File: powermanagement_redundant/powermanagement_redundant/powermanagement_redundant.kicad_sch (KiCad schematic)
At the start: 48 parts, among them J1 Screw_Terminal_01x01, J2 Screw_Terminal_01x01, J3 Screw_Terminal_01x01, J4 Screw_Terminal_01x01, J5 Screw_Terminal_01x01, J6 Screw_Terminal_01x01, J7 Screw_Terminal_01x01, J8 Screw_Terminal_01x01, SW1 SW_DIP_x01, SW2 SW_DIP_x01

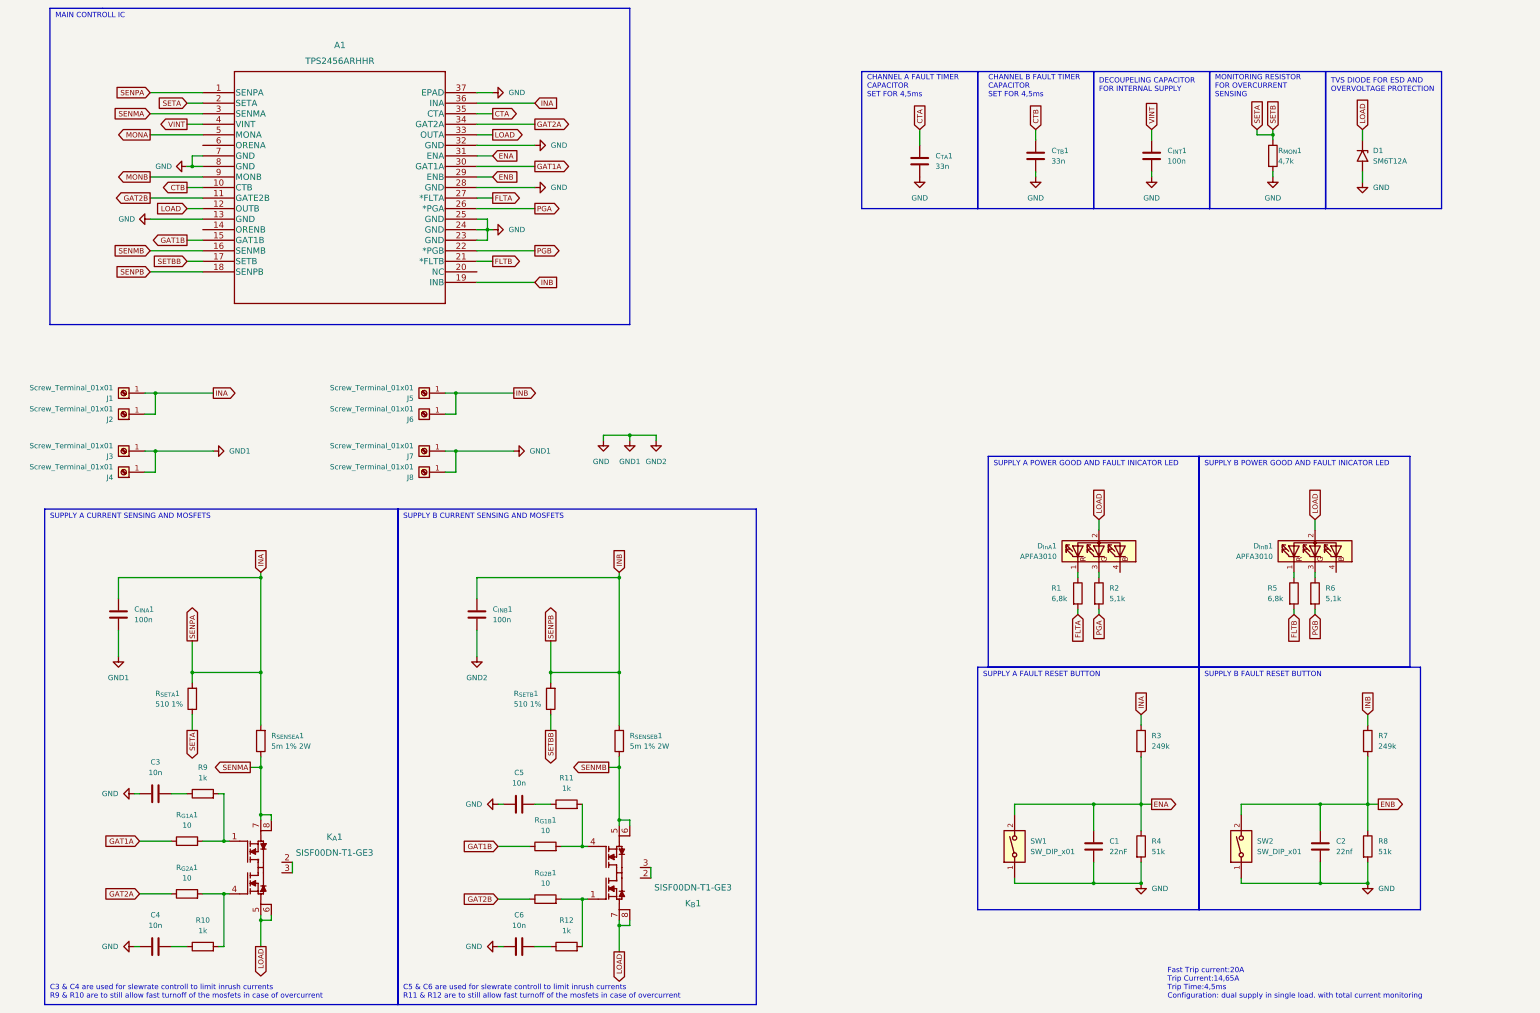
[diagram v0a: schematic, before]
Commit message: add PCB and make it for Aisler work
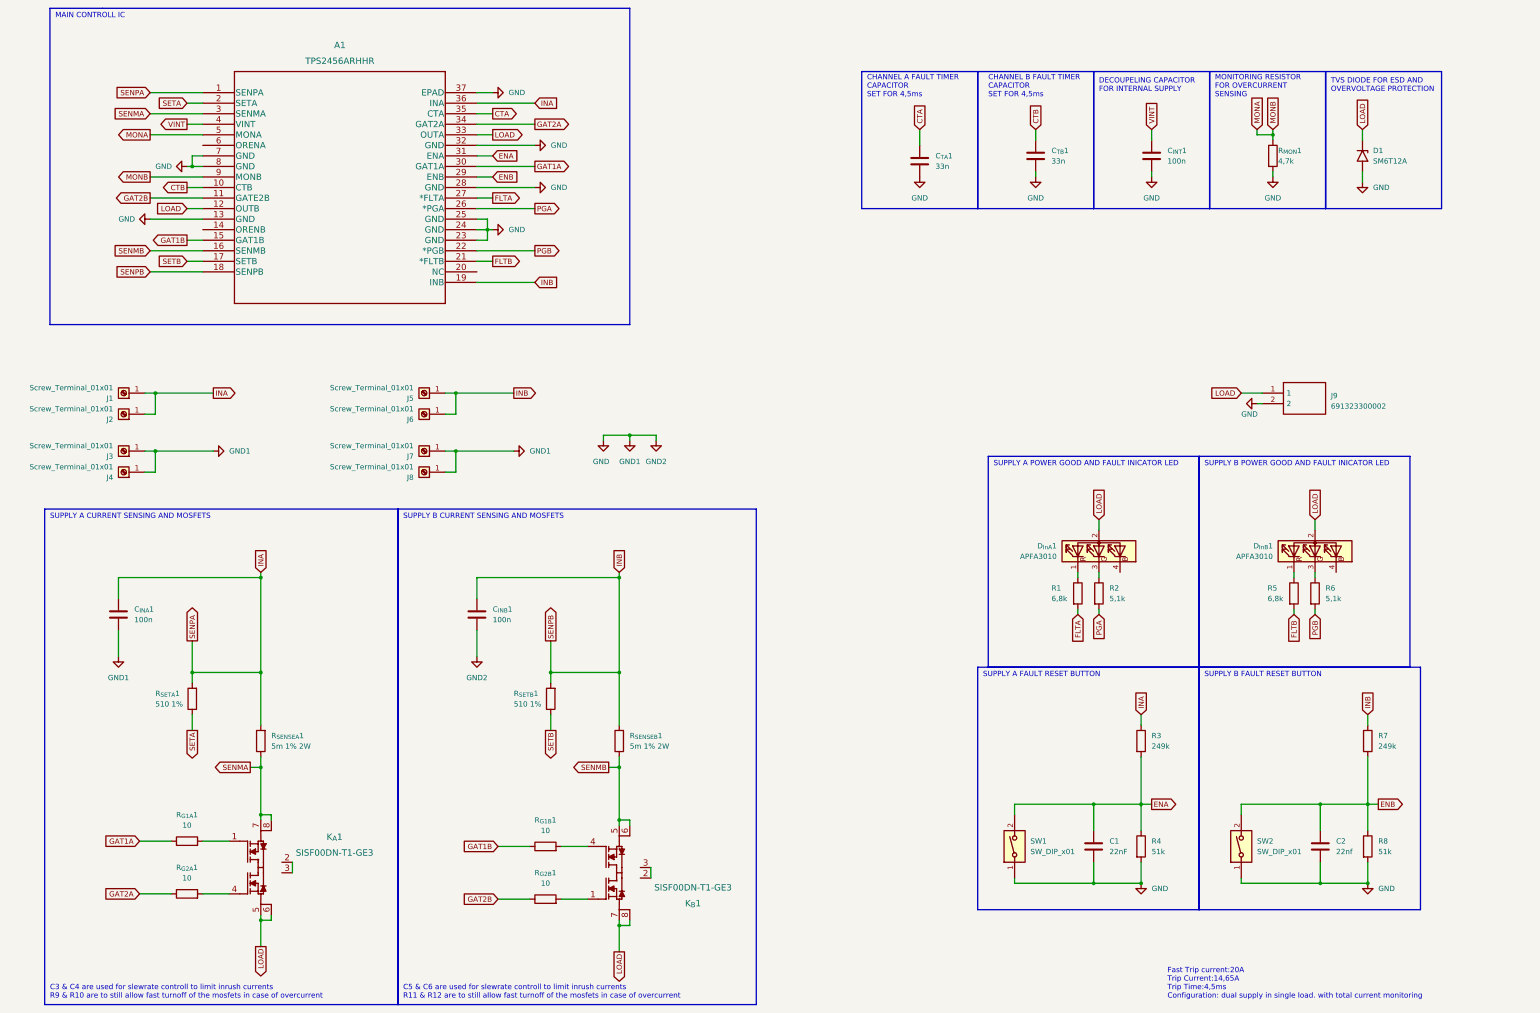
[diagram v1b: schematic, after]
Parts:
- removed C3, C4, C5, C6: 10n, Capacitor_SMD:C_0805_2012Metric_Pad1.18x1.45mm_HandSolder, symbol Device:C
- removed R10, R11, R12, R9: 1k, Resistor_SMD:R_0805_2012Metric_Pad1.20x1.40mm_HandSolder, symbol Device:R
- added J9: 691323300002, KiCad:691323300002, symbol 691323300002:691323300002
- C1, C2, C_{INA}1, C_{INB}1, C_{INT}1, C_{TA}1, C_{TB}1: footprint Capacitor_SMD:C_0805_2012Metric_Pad1.18x1.45mm_HandSolder -> Capacitor_SMD:C_0805_2012Metric
- R1, R2, R3, R4, R5, R6, R7, R8, R_{G1A}1, R_{G1B}1, R_{G2A}1, R_{G2B}1, R_{MON}1, R_{SETA}1, R_{SETB}1: footprint Resistor_SMD:R_0805_2012Metric_Pad1.20x1.40mm_HandSolder -> Resistor_SMD:R_0805_2012Metric
- R_{SENSEA}1, R_{SENSEB}1: footprint Resistor_SMD:R_0612_1632Metric_Pad1.18x3.40mm_HandSolder -> Resistor_SMD:R_0612_1632Metric
- SW1, SW2: footprint Button_Switch_SMD:Panasonic_EVQPUL_EVQPUC -> Button_Switch_SMD:Panasonic_EVQPUK_EVQPUB; Name EVQ-P7C01 -> EVQ-P7B01P
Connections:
- net MONB is gone; now on net MONA: A1.9 (MONB)
- net GND: now also J9.2
- net LOAD: now also J9.1
- net MONA: now also R_{MON}1.1
- net SETA: no longer R_{MON}1.1
- net SETBB renamed SETB

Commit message: upgrade mosfet footprint, change some values
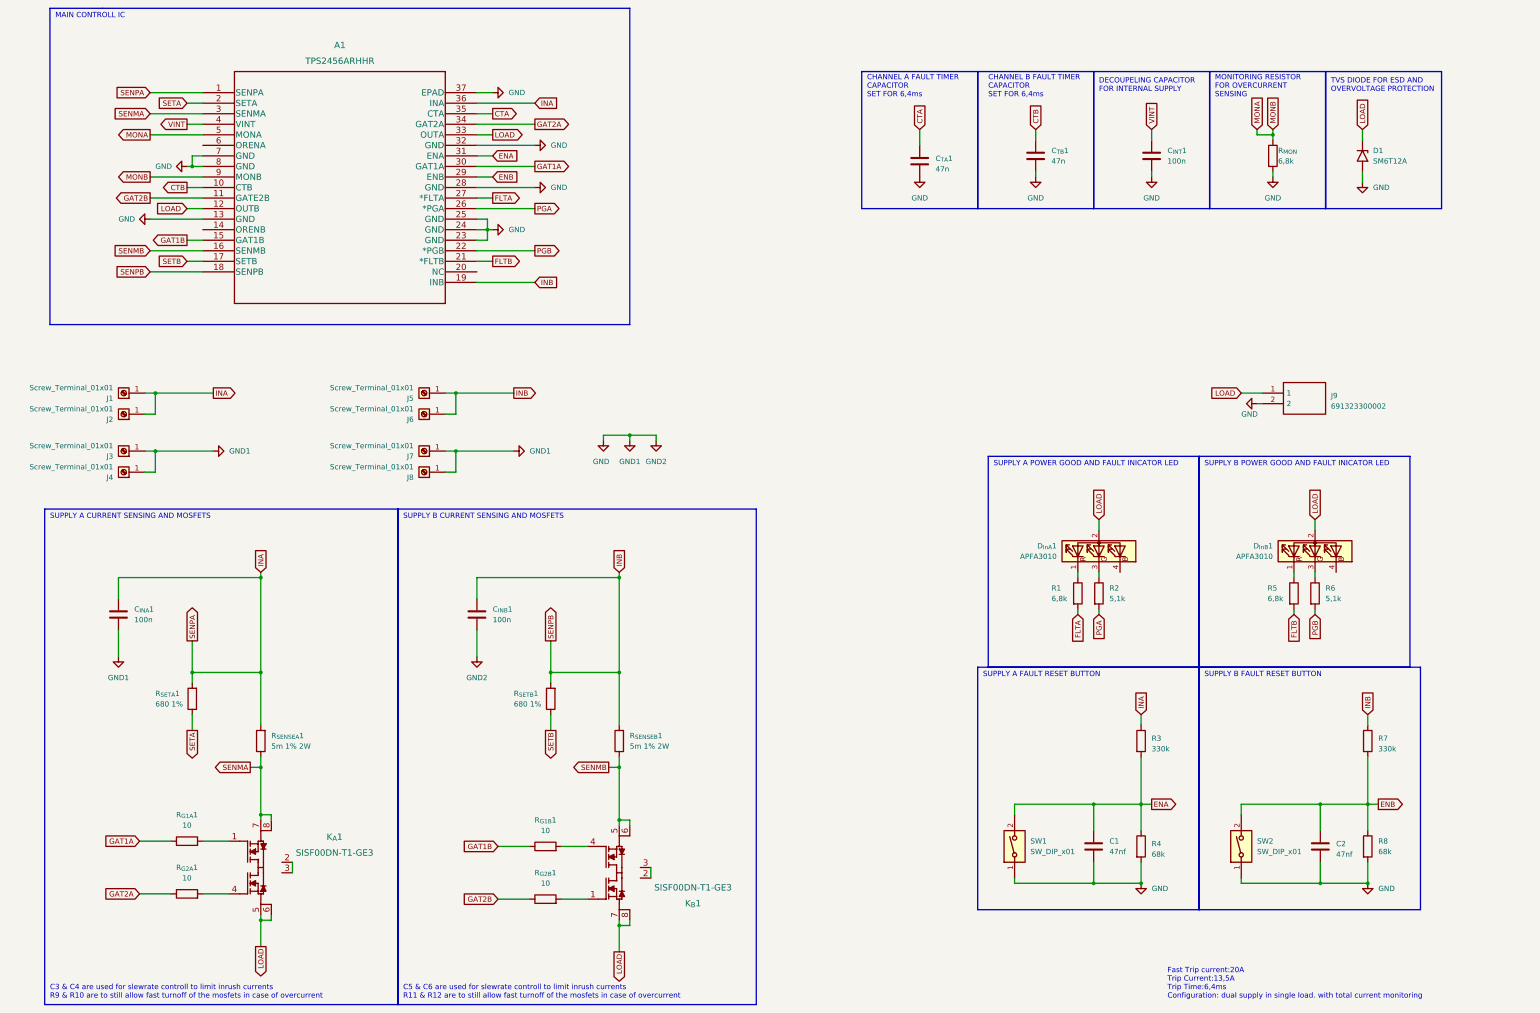
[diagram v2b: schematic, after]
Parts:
- C1: value 22nF -> 47nf
- C2: value 22nf -> 47nf
- C_{TA}1, C_{TB}1: value 33n -> 47n
- R3, R7: value 249k -> 330k
- R4, R8: value 51k -> 68k
- R_{MON}: renamed from R_{MON}1; value 4,7k -> 6,8k
- R_{SETA}1, R_{SETB}1: value 510 1% -> 680 1%
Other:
- note added: "CHANNEL A FAULT TIMER CAPACITOR SET FOR 6,4ms"
- note added: "CHANNEL B FAULT TIMER CAPACITOR SET FOR 6,4ms"
- note added: "Fast Trip current:20A Trip Current:13,5A Trip Time:6,4ms Configuration: dual supply in single load. with total current monitoring"
- note removed: "CHANNEL A FAULT TIMER CAPACITOR SET FOR 4,5ms"
- note removed: "CHANNEL B FAULT TIMER CAPACITOR SET FOR 4,5ms"
- note removed: "Fast Trip current:20A Trip Current:14,65A Trip Time:4,5ms Configuration: dual supply in single load. with total current monitoring"
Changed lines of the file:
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@@
     (stroke (width 0) (type default))
   )
-  (text "CHANNEL A FAULT TIMER \nCAPACITOR\nSET FOR 4,5ms" (at 228.6 45.72 0)
+  (text "CHANNEL A FAULT TIMER \nCAPACITOR\nSET FOR 6,4ms" (at 228.6 45.72 0)
     (effects (font (size 1.27 1.27)) (justify left bottom))
   )
@@
     (effects (font (size 1.27 1.27)) (justify left bottom))
   )
-  (text "Fast Trip current:20A\nTrip Current:14,65A\nTrip Time:4,5ms\nConfiguration: dual supply in single load. with total current monitoring"
+  (text "Fast Trip current:20A\nTrip Current:13,5A\nTrip Time:6,4ms\nConfiguration: dual supply in single load. with total current monitoring"
     (at 300.99 262.89 0)
     (effects (font (size 1.27 1.27)) (justify left bottom))
   )
-  (text "CHANNEL B FAULT TIMER \nCAPACITOR\nSET FOR 4,5ms" (at 257.81 45.72 0)
+  (text "CHANNEL B FAULT TIMER \nCAPACITOR\nSET FOR 6,4ms" (at 257.81 45.72 0)
     (effects (font (size 1.27 1.27)) (justify left bottom))
   )
@@
       (effects (font (size 1.27 1.27)) (justify left))
     )
-    (property "Value" "51k" (at 351.79 227.3299 0)
+    (property "Value" "68k" (at 351.79 227.3299 0)
       (effects (font (size 1.27 1.27)) (justify left))
     )
@@
   (symbol (lib_id "Device:C") (at 337.82 226.06 0) (unit 1)
     (in_bom yes) (on_board yes) (dnp no) (fields_autoplaced)
-    (property "Reference" "C2" (at 341.63 224.7899 0)
-      (effects (font (size 1.27 1.27)) (justify left))
-    )
-    (property "Value" "22nf" (at 341.63 227.3299 0)
+    (property "Reference" "C2" (at 341.63 225.425 0)
+      (effects (font (size 1.27 1.27)) (justify left))
+    )
+    (property "Value" "47nf" (at 341.63 227.965 0)
       (effects (font (size 1.27 1.27)) (justify left))
     )
@@
       (effects (font (size 1.27 1.27)) (justify right))
     )
-    (property "Value" "510 1%" (at 143.51 191.77 0)
+    (property "Value" "680 1%" (at 143.51 191.77 0)
       (effects (font (size 1.27 1.27)) (justify right))
     )
@@
       (effects (font (size 1.27 1.27)) (justify left))
     )
-    (property "Value" "33n" (at 273.05 60.9599 0)
+    (property "Value" "47n" (at 273.05 60.9599 0)
       (effects (font (size 1.27 1.27)) (justify left))
     )
@@
       (effects (font (size 1.27 1.27)) (justify left))
     )
-    (property "Value" "22nF" (at 287.02 227.3299 0)
+    (property "Value" "47nf" (at 287.02 227.3299 0)
       (effects (font (size 1.27 1.27)) (justify left))
     )
@@
   (symbol (lib_id "Device:R") (at 294.64 226.06 0) (unit 1)
     (in_bom yes) (on_board yes) (dnp no) (fields_autoplaced)
-    (property "Reference" "R4" (at 297.18 224.7899 0)
-      (effects (font (size 1.27 1.27)) (justify left))
-    )
-    (property "Value" "51k" (at 297.18 227.3299 0)
+    (property "Reference" "R4" (at 297.18 225.425 0)
+      (effects (font (size 1.27 1.27)) (justify left))
+    )
+    (property "Value" "68k" (at 297.18 227.965 0)
       (effects (font (size 1.27 1.27)) (justify left))
     )
@@
   (symbol (lib_id "Device:C") (at 241.3 60.96 0) (unit 1)
     (in_bom yes) (on_board yes) (dnp no) (fields_autoplaced)
-    (property "Reference" "C_{TA}1" (at 245.11 59.6899 0)
-      (effects (font (size 1.27 1.27)) (justify left))
-    )
-    (property "Value" "33n" (at 245.11 62.2299 0)
+    (property "Reference" "C_{TA}1" (at 245.11 60.325 0)
+      (effects (font (size 1.27 1.27)) (justify left))
+    )
+    (property "Value" "47n" (at 245.11 62.865 0)
       (effects (font (size 1.27 1.27)) (justify left))
     )
@@
   (symbol (lib_id "Device:R") (at 326.39 59.69 0) (unit 1)
     (in_bom yes) (on_board yes) (dnp no)
-    (property "Reference" "R_{MON}1" (at 327.66 58.42 0)
-      (effects (font (size 1.27 1.27)) (justify left))
-    )
-    (property "Value" "4,7k" (at 327.66 60.96 0)
+    (property "Reference" "R_{MON}" (at 327.66 58.42 0)
+      (effects (font (size 1.27 1.27)) (justify left))
+    )
+    (property "Value" "6,8k" (at 327.66 60.96 0)
       (effects (font (size 1.27 1.27)) (justify left))
     )
@@
       (project "powermanagement_redundant"
         (path "/8a7a656b-558d-4577-8c43-8c0fcd36144c"
-          (reference "R_{MON}1") (unit 1)
+          (reference "R_{MON}") (unit 1)
         )
       )
@@
   (symbol (lib_id "Device:R") (at 349.25 200.66 0) (unit 1)
     (in_bom yes) (on_board yes) (dnp no) (fields_autoplaced)
-    (property "Reference" "R7" (at 351.79 199.3899 0)
-      (effects (font (size 1.27 1.27)) (justify left))
-    )
-    (property "Value" "249k" (at 351.79 201.9299 0)
+    (property "Reference" "R7" (at 351.79 200.025 0)
+      (effects (font (size 1.27 1.27)) (justify left))
+    )
+    (property "Value" "330k" (at 351.79 202.565 0)
       (effects (font (size 1.27 1.27)) (justify left))
     )
@@
       (effects (font (size 1.27 1.27)) (justify right))
     )
-    (property "Value" "510 1%" (at 57.15 191.77 0)
+    (property "Value" "680 1%" (at 57.15 191.77 0)
       (effects (font (size 1.27 1.27)) (justify right))
     )
@@
   (symbol (lib_id "Device:R") (at 294.64 200.66 0) (unit 1)
     (in_bom yes) (on_board yes) (dnp no) (fields_autoplaced)
-    (property "Reference" "R3" (at 297.18 199.3899 0)
-      (effects (font (size 1.27 1.27)) (justify left))
-    )
-    (property "Value" "249k" (at 297.18 201.9299 0)
-      (effects (font (size 1.27 1.27)) (justify left))
-    )
+    (property "Reference" "R3" (at 297.18 200.025 0)
+      (effects (font (size 1.27 1.27)) (justify left))
+    )
+    (property "Value" "330k" (at 297.18 202.565 0)
+      (effects (font (size 1.27 1.27)) (justify left))
+    )

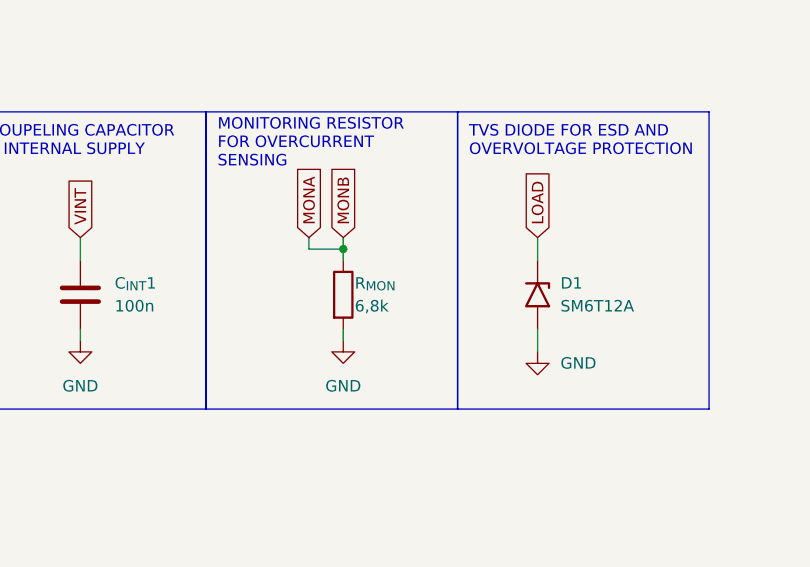
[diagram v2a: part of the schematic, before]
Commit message: Update powermanagement_redundant.kicad_sch
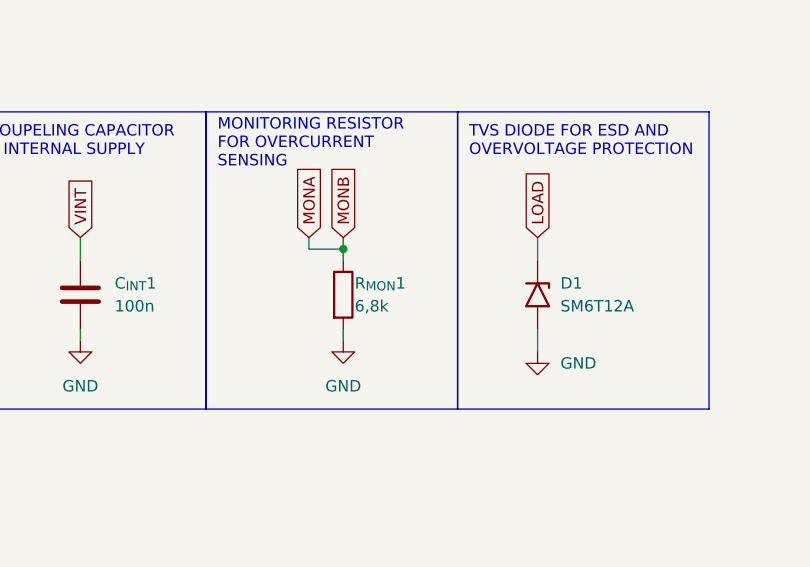
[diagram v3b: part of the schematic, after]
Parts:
- renumbered R_{MON} to R_{MON}1
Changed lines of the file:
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@@
   (symbol (lib_id "Device:R") (at 326.39 59.69 0) (unit 1)
     (in_bom yes) (on_board yes) (dnp no)
-    (property "Reference" "R_{MON}" (at 327.66 58.42 0)
+    (property "Reference" "R_{MON}1" (at 327.66 58.42 0)
       (effects (font (size 1.27 1.27)) (justify left))
     )
@@
       (project "powermanagement_redundant"
         (path "/8a7a656b-558d-4577-8c43-8c0fcd36144c"
-          (reference "R_{MON}") (unit 1)
+          (reference "R_{MON}1") (unit 1)
         )
       )
